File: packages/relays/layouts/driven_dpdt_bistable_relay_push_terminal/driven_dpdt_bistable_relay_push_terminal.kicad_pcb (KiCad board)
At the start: 2 copper layers, 10 parts

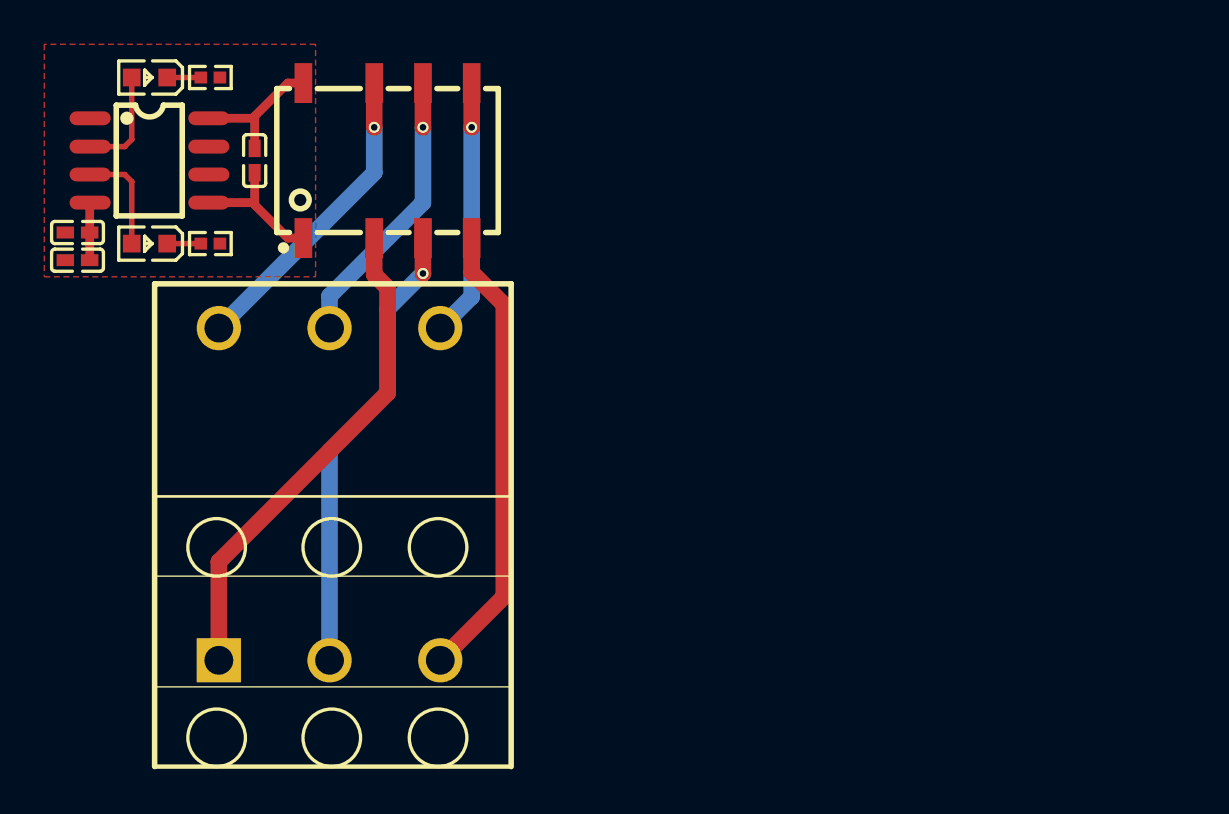
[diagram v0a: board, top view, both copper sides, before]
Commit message: Change name and update layout
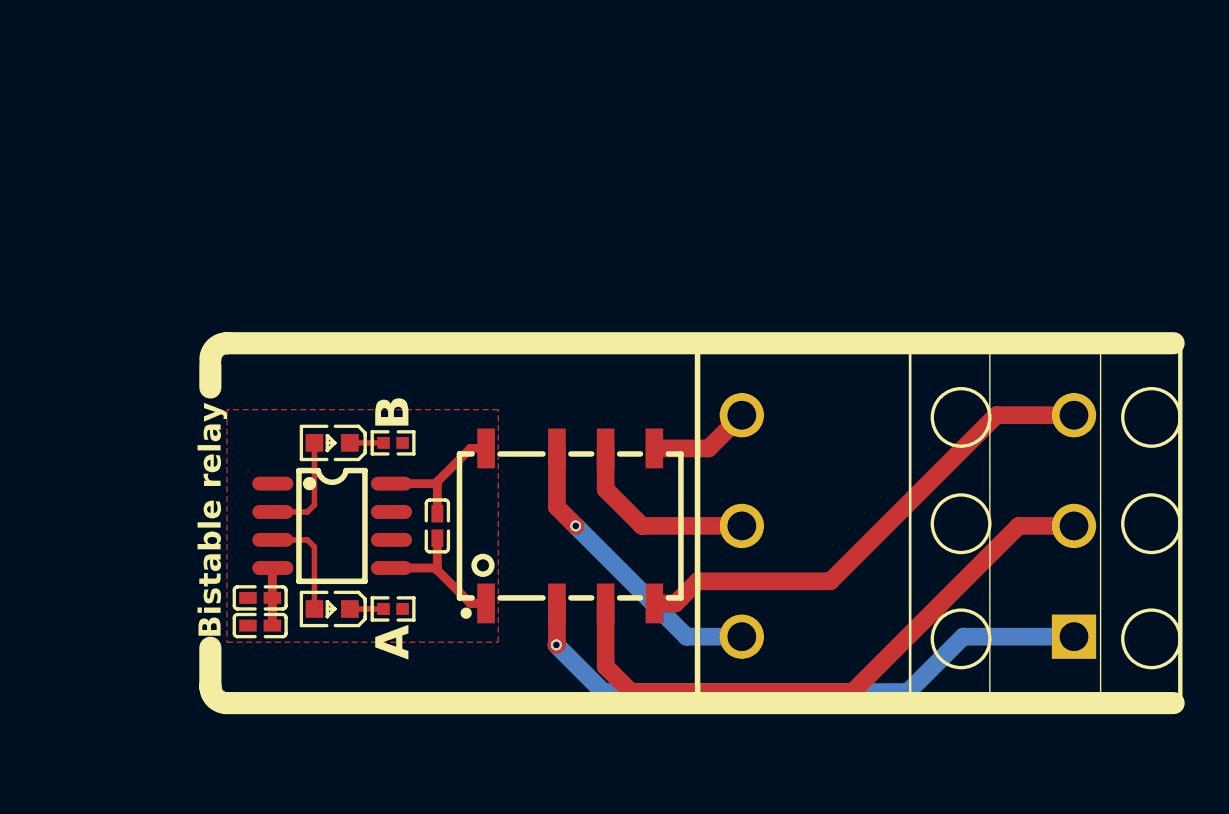
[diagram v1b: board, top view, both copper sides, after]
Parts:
- moved X1 26.2 mm to (26.0, 0.00), turned to 90 degrees
- moved C1 18.4 mm to (-3.25, 3.25)
- moved C2 18.4 mm to (-3.25, 4.50)
- moved C3 18.4 mm to (4.75, 0.00)
- moved D1 18.4 mm to (0.00, -3.75)
- moved D2 18.4 mm to (0.00, 3.75)
- moved R1 18.4 mm to (2.75, -3.75)
- moved R2 18.4 mm to (2.75, 3.75)
- moved RELAY1 18.4 mm to (10.8, 0.00)
- moved U1 18.4 mm to (0.00, 0.00)
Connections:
- C1 pad 2: gnd-1 -> gnd
- C2 pad 2: gnd-1 -> gnd
- C3 pad 2: gnd -> gnd-1
- D1 pad 2: line -> line-1
- D2 pad 2: line-1 -> line
- R1 pad 2: gnd-1 -> gnd
- R2 pad 2: gnd-1 -> gnd
- RELAY1 pad 1: gnd -> gnd-1
- U1 pad 2: line -> line-1
- U1 pad 3: line-1 -> line
- U1 pad 5: gnd -> gnd-1
- U1 pad 6: gnd-1 -> gnd
- U1 pad 7: gnd-1 -> gnd
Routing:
- net PB3: track 11.7 -> 4.57 mm, vias 1 -> 0
- net PA2: track 20.8 -> 27.6 mm, vias 1 -> 0
- net gnd-1: track 0.00 -> 6.34 mm
- net gnd: track 6.34 -> 0.00 mm
- net PA1: track 22.5 -> 27.2 mm, vias 0 -> 1
- net PB2: track 12.8 -> 8.68 mm, vias 1 -> 0
- net PA3: track 20.9 -> 22.5 mm
- net PB1: track 14.0 -> 13.4 mm
- added copper zone on F.Cu, net gnd
- removed copper zone on F.Cu, net gnd-1
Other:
- board text added: "A"
- board text added: "B"
- board text added: "Bistable relay"

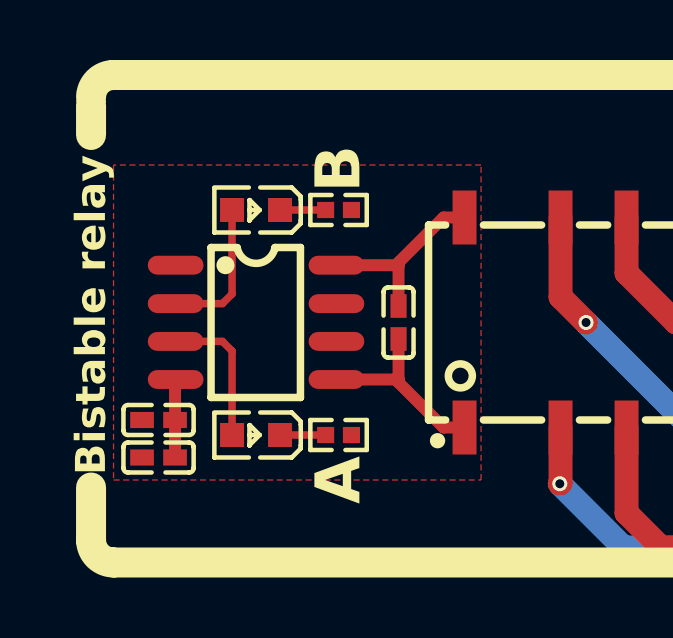
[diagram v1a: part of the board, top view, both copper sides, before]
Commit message: Rebuild relays package
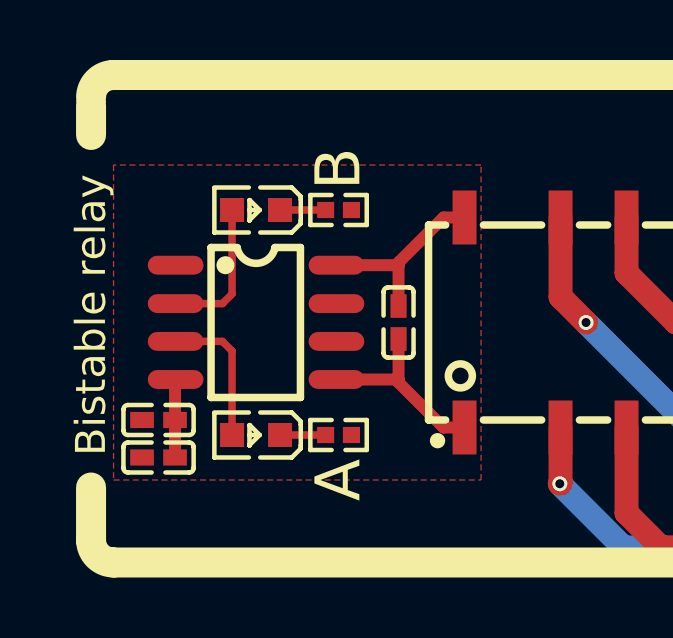
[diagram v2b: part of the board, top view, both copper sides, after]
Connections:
- D1 pad 2: line-1 -> line
- D2 pad 2: line -> line-1
- U1 pad 2: line-1 -> line
- U1 pad 3: line -> line-1

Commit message: Rebuild all
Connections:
- C1 pad 2: gnd -> gnd-1
- C2 pad 2: gnd -> gnd-1
- C3 pad 2: gnd-1 -> gnd
- R1 pad 2: gnd -> gnd-1
- R2 pad 2: gnd -> gnd-1
- RELAY1 pad 1: gnd-1 -> gnd
- U1 pad 5: gnd-1 -> gnd
- U1 pad 6: gnd -> gnd-1
- U1 pad 7: gnd -> gnd-1
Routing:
- net gnd-1: track 6.34 -> 0.00 mm
- net gnd: track 0.00 -> 6.34 mm
- added copper zone on F.Cu, net gnd-1
- removed copper zone on F.Cu, net gnd
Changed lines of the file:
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@@
     )
     (net 0 "")
-    (net 1 "gnd-1")
+    (net 1 "gnd")
     (net 2 "relay.led_indicator_a.led-cathode")
     (net 3 "line-1")
@@
     (net 7 "net")
     (net 8 "hv")
-    (net 9 "gnd")
+    (net 9 "gnd-1")
     (net 10 "PA2")
     (net 11 "PB2")
@@
             (size 0.57 0.54)
             (layers "F.Cu" "F.Mask" "F.Paste")
-            (net 9 "gnd")
+            (net 9 "gnd-1")
         )
         (embedded_fonts no)
@@
             (size 0.79 0.54)
             (layers "F.Cu" "F.Mask" "F.Paste")
-            (net 9 "gnd")
+            (net 9 "gnd-1")
         )
         (embedded_fonts no)
@@
             (size 0.63 1.86)
             (layers "F.Cu" "F.Mask" "F.Paste")
-            (net 1 "gnd-1")
+            (net 1 "gnd")
         )
         (pad "6" smd oval
@@
             (size 0.63 1.86)
             (layers "F.Cu" "F.Mask" "F.Paste")
-            (net 9 "gnd")
+            (net 9 "gnd-1")
         )
         (pad "7" smd oval
@@
             (size 0.63 1.86)
             (layers "F.Cu" "F.Mask" "F.Paste")
-            (net 9 "gnd")
+            (net 9 "gnd-1")
         )
         (pad "8" smd oval
@@
             (size 0.8 1.8)
             (layers "F.Cu" "F.Mask" "F.Paste")
-            (net 1 "gnd-1")
+            (net 1 "gnd")
         )
         (pad "2" smd rect
@@
             (size 0.57 0.54)
             (layers "F.Cu" "F.Mask" "F.Paste")
-            (net 9 "gnd")
+            (net 9 "gnd-1")
         )
         (embedded_fonts no)
@@
             (size 0.79 0.54)
             (layers "F.Cu" "F.Mask" "F.Paste")
-            (net 9 "gnd")
+            (net 9 "gnd-1")
         )
         (embedded_fonts no)
@@
             (size 0.79 0.54)
             (layers "F.Cu" "F.Mask" "F.Paste")
-            (net 1 "gnd-1")
+            (net 1 "gnd")
         )
         (embedded_fonts no)
@@
     (zone
         (net 9)
-        (net_name "gnd")
+        (net_name "gnd-1")
         (layers "F.Cu")
         (hatch edge 0.5)

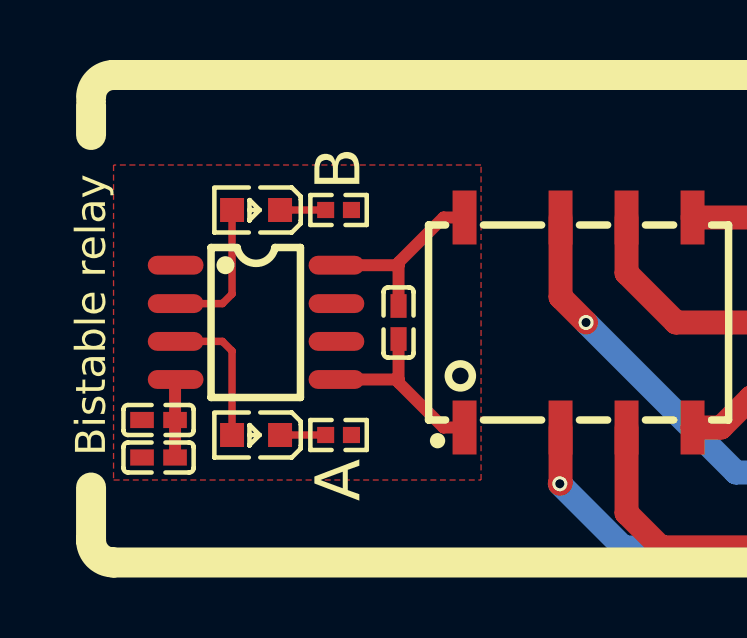
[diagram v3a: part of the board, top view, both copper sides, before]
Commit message: Fix wrong logic reference. Split driver into own module
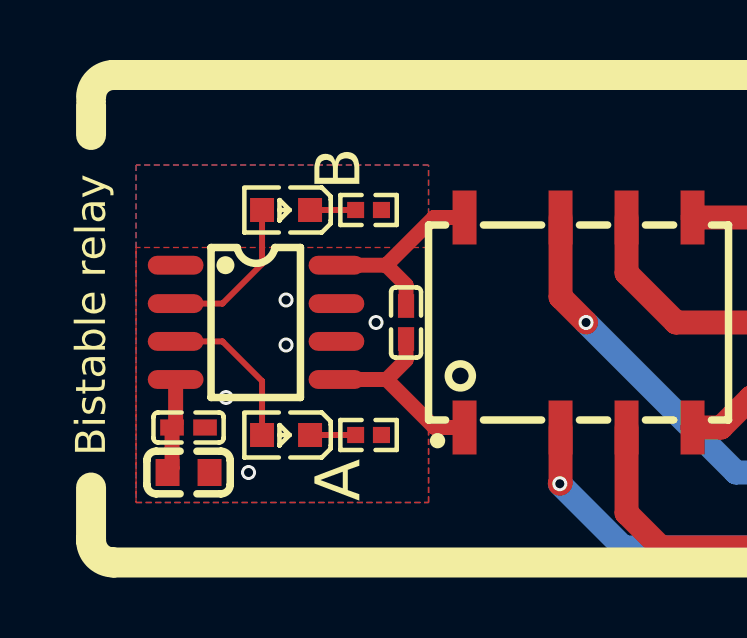
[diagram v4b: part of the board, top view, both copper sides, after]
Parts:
- C2: value 100nF ±10% 16V X7R -> 4.7µF ±10% 16V X5R; footprint atopile:C0402-b3ef17 -> atopile:C0603-bd72f6
- C3: value 100nF ±10% 16V X7R -> 100pF ±5% 50V C0G
- R1, R2: value 100kΩ ±1% 62.5mW -> 1kΩ ±1% 62.5mW
- moved C2 1.12 mm to (-2.25, 5.00), turned to 0 degrees
- moved C1 1.03 mm to (-2.25, 3.50), turned to 0 degrees
- moved D1 1.00 mm to (1.00, -3.75)
- moved D2 1.00 mm to (1.00, 3.75)
- moved R1 1.00 mm to (3.75, -3.75)
- moved R2 1.00 mm to (3.75, 3.75)
- moved C3 0.25 mm to (5.00, 0.00)
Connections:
- C1 pad 1: hv-1 -> hv
- C1 pad 2: gnd-1 -> gnd
- C2 pad 1: hv-1 -> hv
- C2 pad 2: gnd-1 -> gnd
- C3 pad 1: hv -> OUTA
- C3 pad 2: gnd -> relay-gnd
- D1 pad 2: line -> line-1
- D2 pad 2: line-1 -> line
- R1 pad 2: gnd-1 -> gnd
- R2 pad 2: gnd-1 -> gnd
- RELAY1 pad 1: gnd -> relay-gnd
- RELAY1 pad 8: hv -> OUTA
- U1 pad 2: line -> line-1
- U1 pad 3: line-1 -> line
- U1 pad 4: hv-1 -> hv
- U1 pad 5: gnd -> relay-gnd
- U1 pad 6: gnd-1 -> gnd
- U1 pad 7: gnd-1 -> gnd
- U1 pad 8: hv -> OUTA
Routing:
- net OUTA: track 0.00 -> 6.56 mm
- net relay-gnd: track 0.00 -> 6.55 mm
- net gnd: track 6.34 -> 0.00 mm, vias 0 -> 5
- net hv: track 6.34 -> 3.21 mm
- net hv-1: track 2.61 -> 0.00 mm
- added copper zone on B.Cu, net gnd
- added copper zone on F.Cu, net gnd
- removed copper zone on F.Cu, net gnd-1

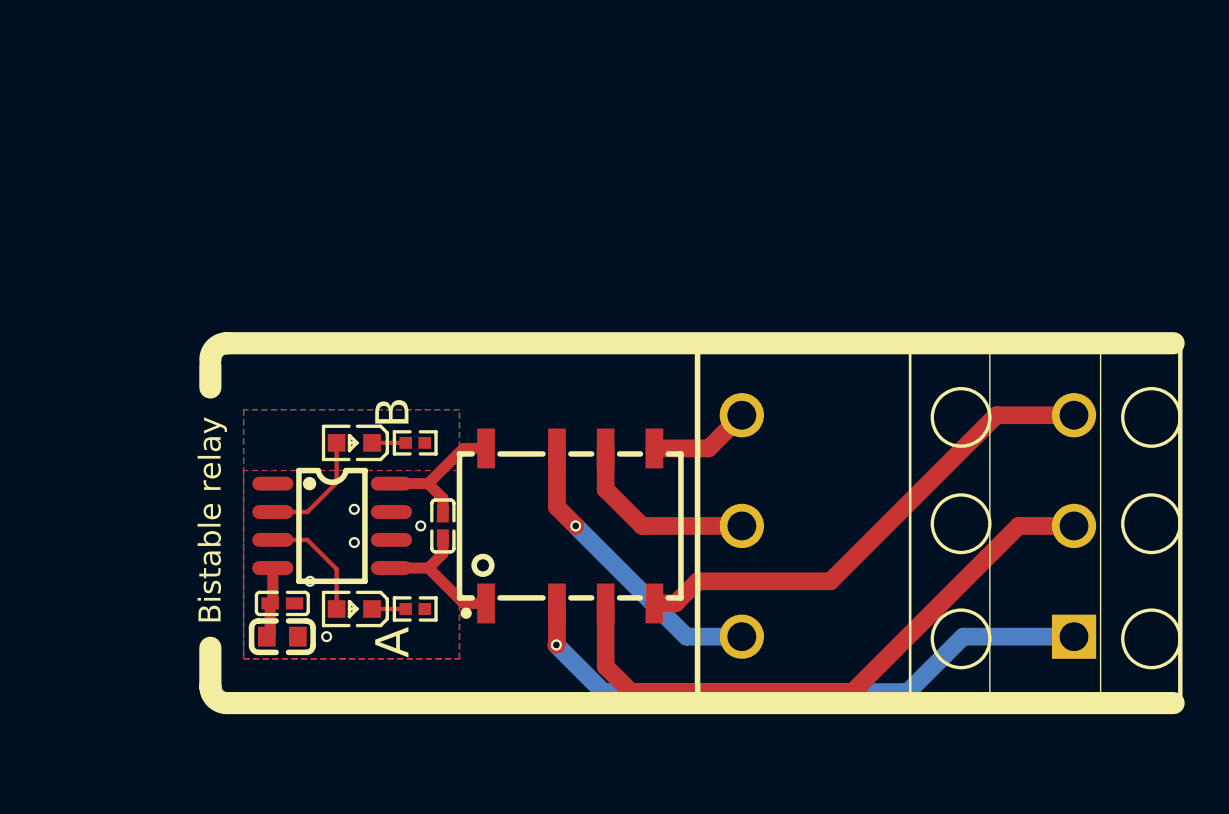
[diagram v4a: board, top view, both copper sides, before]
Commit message: Update packages to ato v0.9.x (#36)
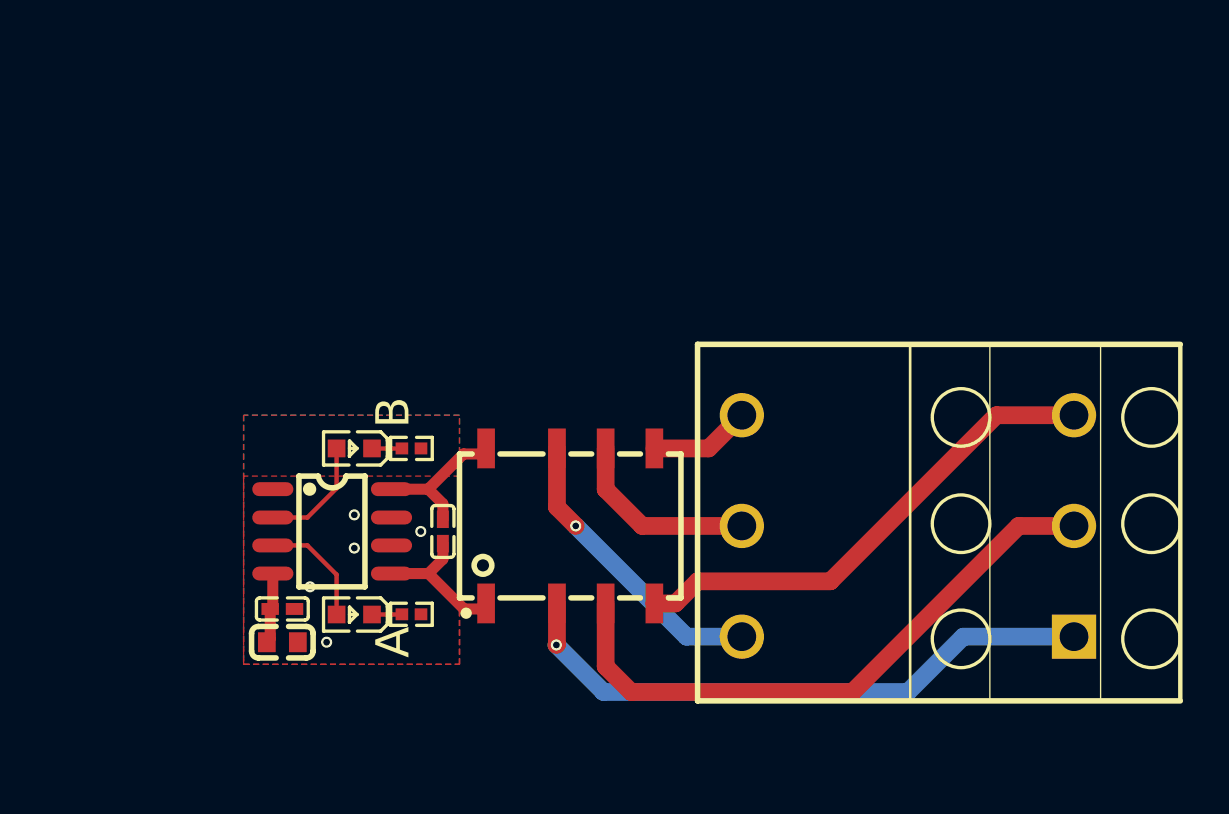
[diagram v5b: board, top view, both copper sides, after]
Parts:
- removed D1, D2: , atopile:LED0603-RD-c81ffb
- removed RELAY1: , atopile:RELAY-SMD_G6KU-2F-Y-bd7654
- removed X1: , atopile:CONN-TH_KF250T-5.0-2X3P-058638
- added CN1: , Cixi_Kefa_Elec_KF250T_5_0_2_3P:CONN-TH_KF250T-5.0-2X3P, F.Cu at (26.0, 0.00)
- added LED1: , Hubei_KENTO_Elec_KT_0603R:LED0603-RD, F.Cu at (1.00, -3.50)
- added LED2: , Hubei_KENTO_Elec_KT_0603G:LED0603-RD, F.Cu at (1.00, 4.00)
- added U2: , Omron_Electronics_G6KU_2F_Y_TR_DC5:RELAY-SMD_G6KU-2F-Y, F.Cu at (10.8, 0.00)
- C1: footprint atopile:C0402-b3ef17 -> Samsung_Electro_Mechanics_CL05B104KO5NNNC:C0402
- C2: footprint atopile:C0603-bd72f6 -> Samsung_Electro_Mechanics_CL10A475KO8NNNC:C0603
- C3: footprint atopile:C0402-b3ef17 -> FH_0402CG101J500NT:C0402
- R1, R2: value 1kΩ ±1% 62.5mW -> 10kΩ ±1% 62.5mW; footprint atopile:R0402-56259e -> UNI_ROYAL_0402WGF1002TCE:R0402
- U1: footprint atopile:SOP-8_L4.9-W3.9-P1.27-LS6.0-BL-0d1ac6 -> Shenzhen_Fuman_Elec_TC118S:SOP-8_L4.9-W3.9-P1.27-LS6.0-BL
- moved R1 0.30 mm to (3.58, -3.50)
- moved R2 0.29 mm to (3.58, 3.99)
- moved C1 0.25 mm to (-2.25, 3.75)
- moved C2 0.25 mm to (-2.25, 5.25)
- moved C3 0.25 mm to (5.00, 0.25)
- moved U1 0.25 mm to (0.00, 0.25)
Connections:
- R1 pad 1: relay.led_indicator_a.led-cathode -> cathode
- R2 pad 1: relay.led_indicator_b.led-cathode -> cathode-1
- U1 pad 2: line-1 -> anode
- U1 pad 3: line -> anode-1
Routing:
- net PA2: track 27.6 -> 0.00 mm
- net line-2: track 0.00 -> 27.2 mm, vias 0 -> 1
- net PA1: track 27.2 -> 0.00 mm, vias 1 -> 0
- net line-4: track 0.00 -> 22.5 mm
- net PA3: track 22.5 -> 0.00 mm
- net line: track 5.23 -> 27.6 mm
- net line-3: track 0.00 -> 13.4 mm, vias 0 -> 1
- net PB1: track 13.4 -> 0.00 mm, vias 1 -> 0
- net PB2: track 8.68 -> 0.00 mm
- net anode-1: track 0.00 -> 5.23 mm
- net anode: track 0.00 -> 5.23 mm
- net line-5: track 0.00 -> 4.57 mm
- net PB3: track 4.57 -> 0.00 mm
- net line-1: track 5.23 -> 8.68 mm
- net relay.led_indicator_b.led-cathode: track 1.52 -> 0.00 mm
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- added copper zone on F.Cu, net (none)
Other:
- board text removed: "Bistable relay"
